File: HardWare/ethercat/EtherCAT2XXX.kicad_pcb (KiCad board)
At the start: 4 copper layers, 153 parts, among them CN1 5019530507, CN2 5019530507, J1 Conn_01x02, J2 Conn_01x03, J3 Conn_01x04, J4 Conn_01x02, J5 Conn_01x02, J6 Conn_01x03, J7 Conn_01x04, SW1 SW_Push, U1 SY8303AAIC, U2 RT8075, U3 SRV05-4, U4 SRV05-4, U5 STM32F407VETx, U6 TJA1051T-3, U7 TJA1051T-3, U8 AX58100-LQPF80, U9 BL24C16F-PARC, X1 25M, Y1 8M, Y2 32.768KHz

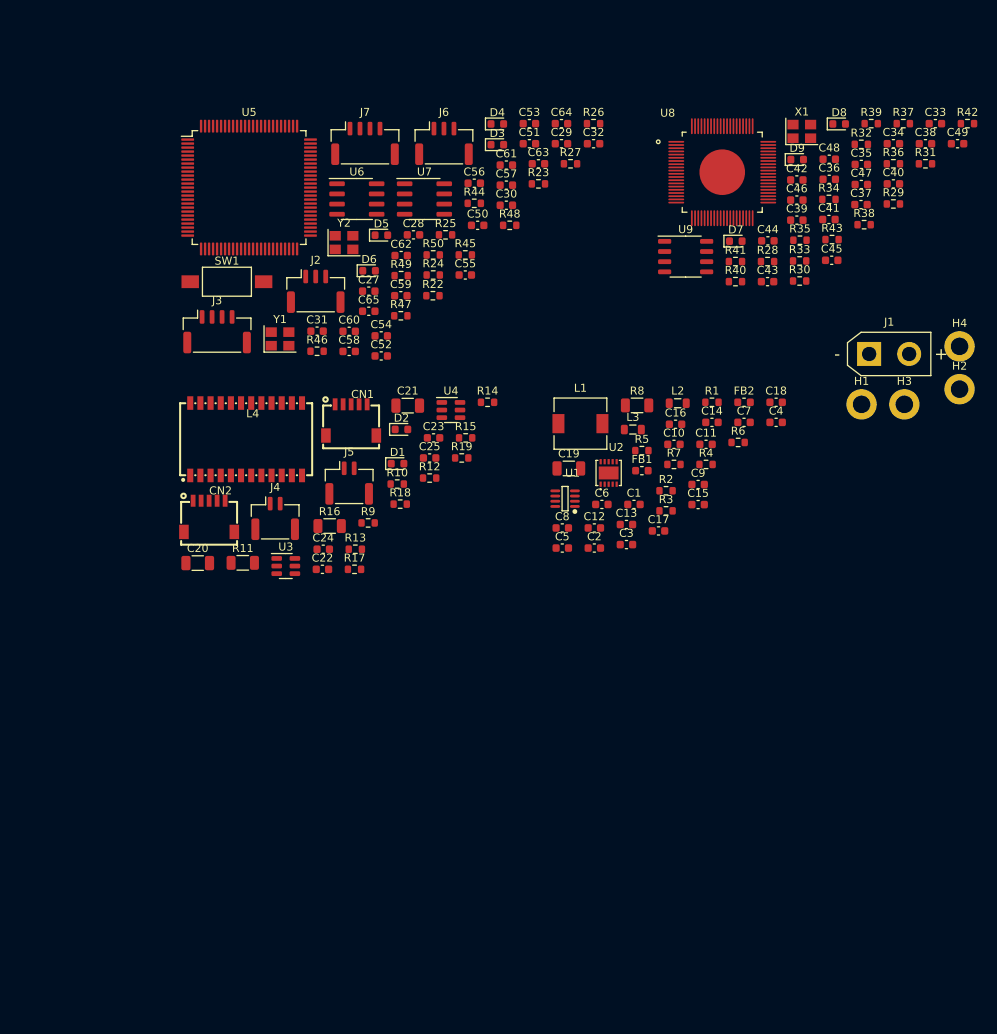
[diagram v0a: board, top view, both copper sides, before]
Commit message: 'ethercat_shield' PCB_layout completed
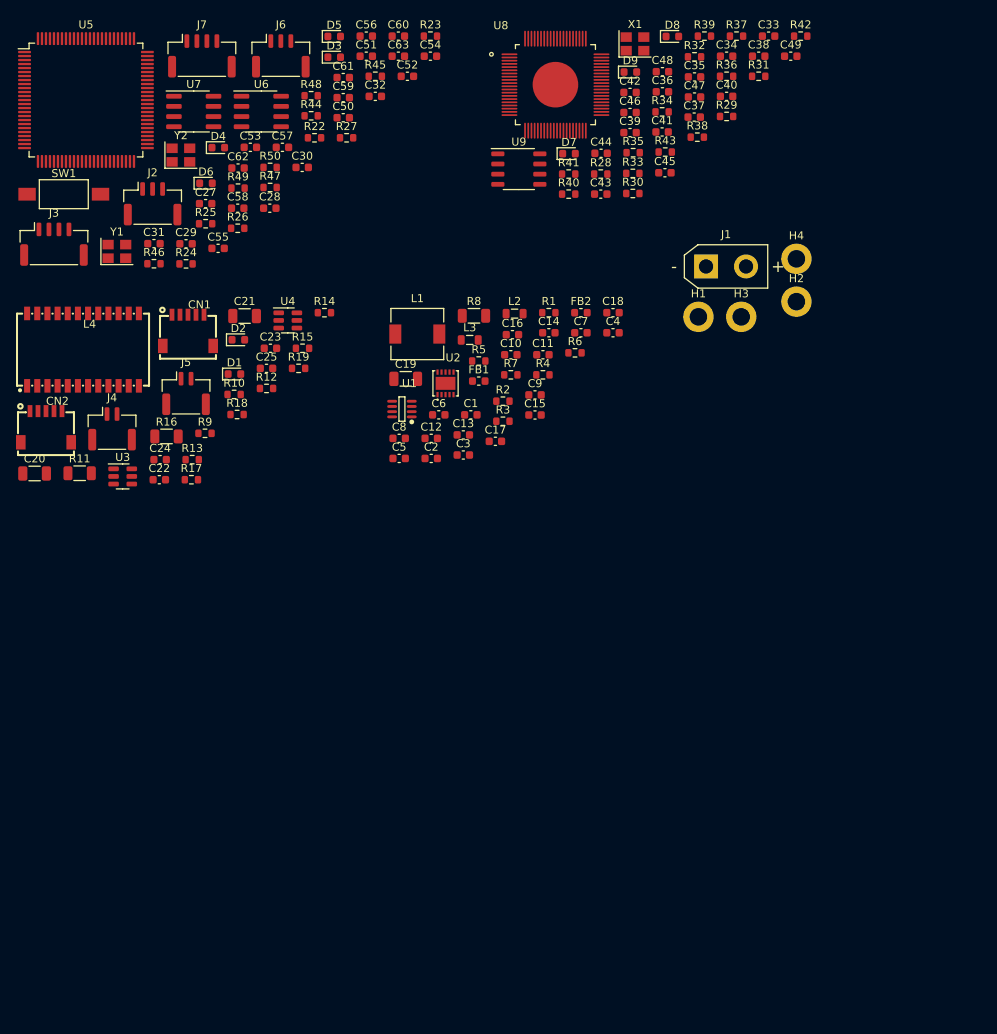
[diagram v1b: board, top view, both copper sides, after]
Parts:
- removed C64, C65: 100n, Capacitor_SMD:C_0603_1608Metric
- moved C29 48.6 mm to (40.5, 41.7)
- moved R26 46.4 mm to (46.9, 39.8)
- moved C60 37.4 mm to (67.0, 15.7)
- moved C54 35.5 mm to (71.0, 18.2)
- moved C52 35.1 mm to (68.1, 20.8)
- moved D4 35.0 mm to (44.5, 29.7)
- moved C53 35.0 mm to (48.5, 29.6)
- moved C55 31.1 mm to (44.5, 42.3)
- moved R24 30.9 mm to (40.5, 44.2)
- moved U7 30.8 mm to (41.4, 25.1)
- moved R25 30.0 mm to (42.9, 39.2)
- moved R48 29.6 mm to (56.1, 23.2)
- moved C57 28.4 mm to (52.5, 29.6)
- moved R27 28.2 mm to (60.5, 28.4)
- moved C32 27.9 mm to (64.1, 23.3)
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
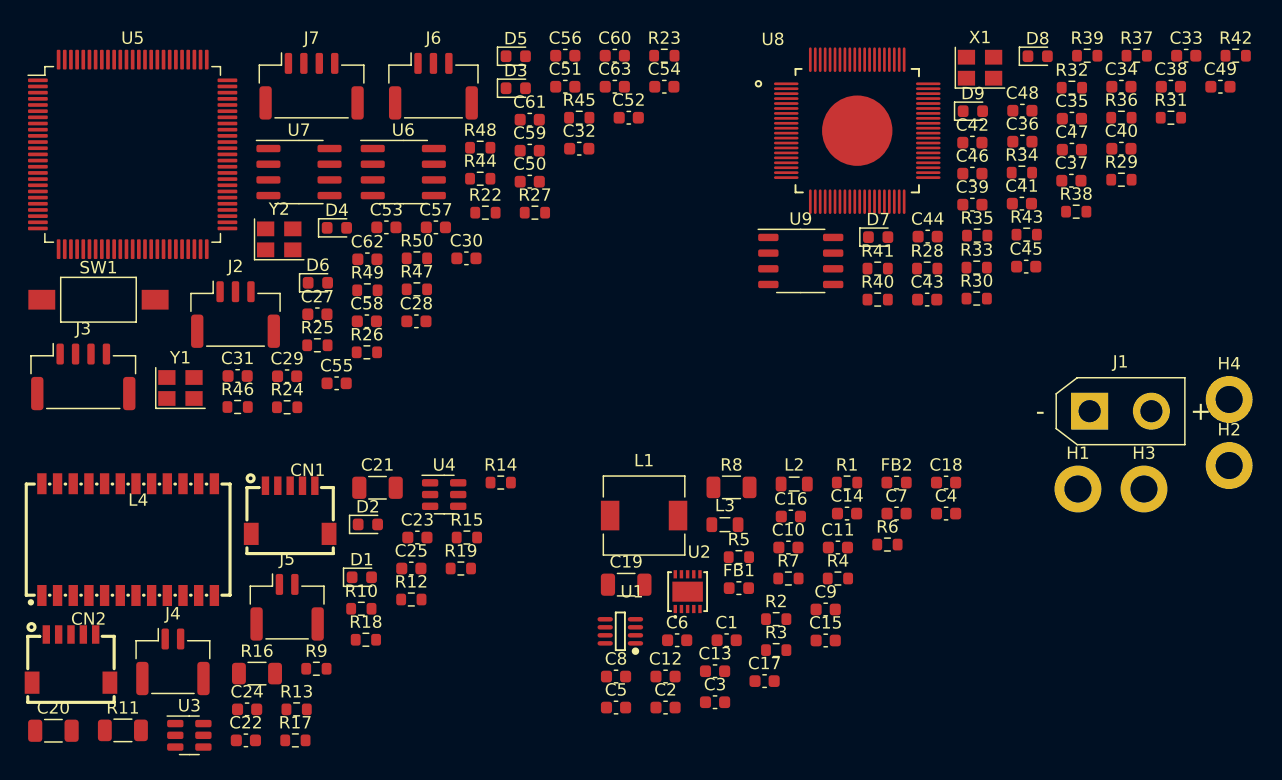
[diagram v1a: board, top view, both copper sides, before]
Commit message: Adaption for Kicad 7.0
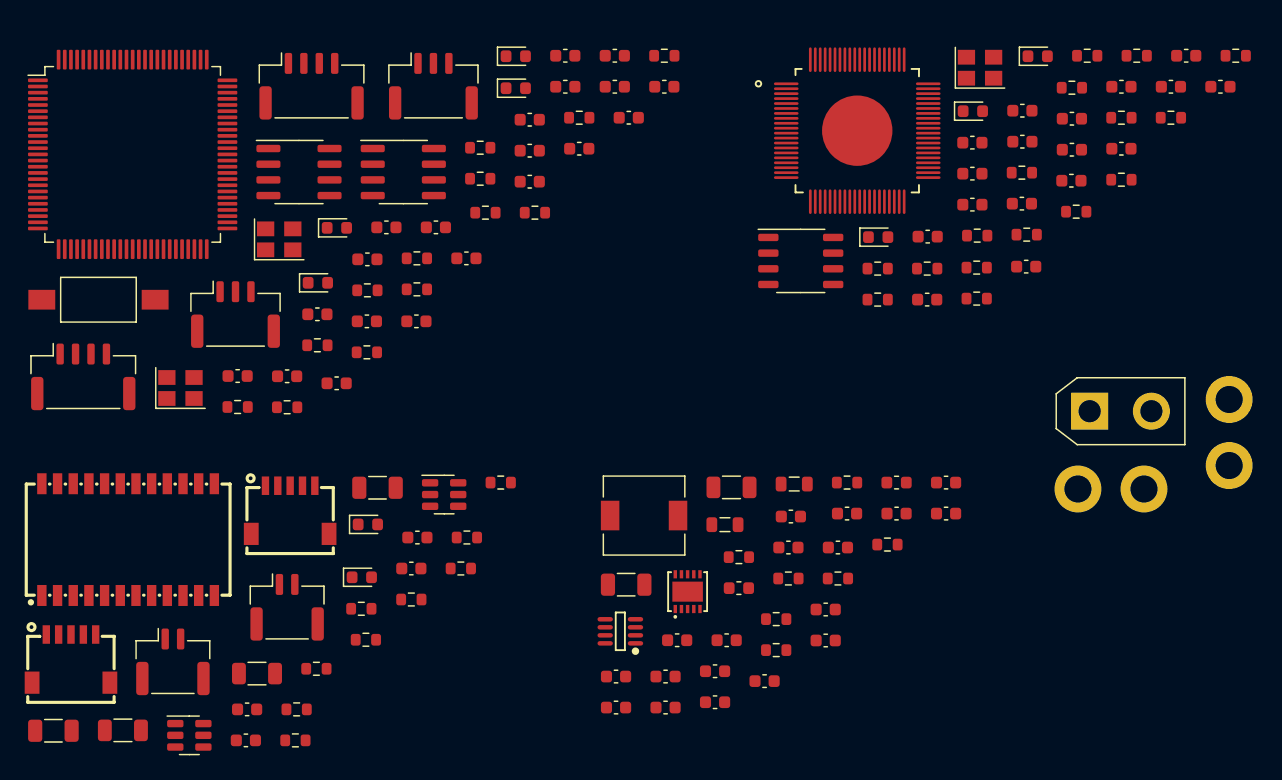
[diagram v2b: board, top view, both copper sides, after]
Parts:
- C35, C36, C37, C38, C39, C40, C41, C42, C43, C44, C45, C46, C47, C48, C49: value 100nF -> 100n

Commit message: Official version-EtherCAT2CAN_NUC
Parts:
- removed C3: 10n, Capacitor_SMD:C_0603_1608Metric
- removed C4: 22u, Capacitor_SMD:C_0603_1608Metric
- removed C50, C51: 2.2u, Capacitor_SMD:C_0603_1608Metric
- removed C52, C54: 10u, Capacitor_SMD:C_0603_1608Metric
- removed C53, C59, C61: 100n, Capacitor_SMD:C_0603_1608Metric
- removed C55, C56: 10p, Capacitor_SMD:C_0603_1608Metric
- removed H1, H2, H4: MountingHole, MountingHole:MountingHole_2.2mm_M2_DIN965_Pad
- removed the H3 at (109.9, 50.8)
- removed J2: Conn_01x03, Connector_JST:JST_GH_SM03B-GHS-TB_1x03-1MP_P1.25mm_Horizontal
- removed J3, J7: Conn_01x04, Connector_JST:JST_GH_SM04B-GHS-TB_1x04-1MP_P1.25mm_Horizontal
- removed L1: 22uH, Inductor_SMD:L_6.3x6.3_H3
- removed R25: 1K, Resistor_SMD:R_0603_1608Metric
- removed R44, R48, R49: 10K, Resistor_SMD:R_0603_1608Metric
- removed R45: 10, Resistor_SMD:R_0603_1608Metric
- removed R46, R47: 0, Resistor_SMD:R_0603_1608Metric
- removed R50: 1M, Resistor_SMD:R_0603_1608Metric
- removed SW1: SW_Push, Button_Switch_SMD:SW_SPST_FSMSM
- removed Y2: 32.768KHz, Crystal:Crystal_SMD_3225-4Pin_3.2x2.5mm
- added C64: 100n, Capacitor_SMD:C_0402_1005Metric, B.Cu at (117.2, 97.6)
- added D10: RED, LED_SMD:LED_0402_1005Metric, F.Cu at (100.6, 128.6)
- added D11: RED, LED_SMD:LED_0402_1005Metric, F.Cu at (101.6, 128.6)
- added D12: BV05C, Diode_SMD:D_SOD-323, F.Cu at (96.3, 129.6)
- added H3: MountingHole, MountingHole:MountingHole_2.7mm_M2.5, F.Cu at (127.3, 93.9)
- added H3: MountingHole, MountingHole:MountingHole_2.7mm_M2.5, F.Cu at (90.3, 93.9)
- added H3: MountingHole, MountingHole:MountingHole_2.7mm_M2.5, F.Cu at (90.3, 134.7)
- added H3: MountingHole, MountingHole:MountingHole_2.7mm_M2.5, F.Cu at (127.4, 134.6)
- added U10: STM32F412RETx, Package_QFP:LQFP-64_10x10mm_P0.5mm, F.Cu at (102.5, 104.8)
- added U11: ~, Package_TO_SOT_SMD:SOT-23-3, F.Cu at (114.5, 96.3)
- C1: value 4.7u -> 100n; footprint Capacitor_SMD:C_0603_1608Metric -> Capacitor_SMD:C_0402_1005Metric; moved to B.Cu
- C10, C13, C14, C17, C18, C27, C28, C32, C46, C6, C8, C9: footprint Capacitor_SMD:C_0603_1608Metric -> Capacitor_SMD:C_0402_1005Metric
- C2: value 10n -> 4.7u; footprint Capacitor_SMD:C_0603_1608Metric -> Capacitor_SMD:C_0402_1005Metric; moved to B.Cu
- C21, R10, R16, R17, R18, R19, R9, U6, U7, U9: moved to B.Cu
- C22, C23, C24, C25, C29, C30, C31, C35, C36, C37, C38, C39, C40, C41, C42, C43, C44, C45, C47, C48, C49, C57, C58, C60, C62, C63: footprint Capacitor_SMD:C_0603_1608Metric -> Capacitor_SMD:C_0402_1005Metric; moved to B.Cu
- C33, C34: value 100nF -> 100n; footprint Capacitor_SMD:C_0603_1608Metric -> Capacitor_SMD:C_0402_1005Metric; moved to B.Cu
- D1, D2: value LED -> GREEN; footprint LED_SMD:LED_0603_1608Metric -> LED_SMD:LED_0402_1005Metric
- D3, D4, D7, D8, D9: footprint LED_SMD:LED_0603_1608Metric -> LED_SMD:LED_0402_1005Metric
- D5: value GREEN -> BLUE; footprint LED_SMD:LED_0603_1608Metric -> LED_SMD:LED_0402_1005Metric
- D6: value GREEN -> BV05C; footprint LED_SMD:LED_0603_1608Metric -> Diode_SMD:D_SOD-323
- J1: value Conn_01x02 -> Conn_01x04; footprint Connector_AMASS:AMASS_XT30UPB-M_1x02_P5.0mm_Vertical -> Connector_JST:JST_GH_SM04B-GHS-TB_1x04-1MP_P1.25mm_Horizontal
- J6: value Conn_01x03 -> Conn_01x06; footprint Connector_JST:JST_GH_SM03B-GHS-TB_1x03-1MP_P1.25mm_Horizontal -> Connector_JST:JST_GH_SM06B-GHS-TB_1x06-1MP_P1.25mm_Horizontal
- R1: value 100K -> 10K; footprint Resistor_SMD:R_0603_1608Metric -> Resistor_SMD:R_0402_1005Metric; moved to B.Cu
- R12, R13, R14, R15, R28, R29, R31, R39, R40, R41, R42, R43: footprint Resistor_SMD:R_0603_1608Metric -> Resistor_SMD:R_0402_1005Metric; moved to B.Cu
- R2: value 150K -> 1K; footprint Resistor_SMD:R_0603_1608Metric -> Resistor_SMD:R_0402_1005Metric
- R22, R23, R24, R26, R27, R30, R32, R33, R34, R35, R36, R37: footprint Resistor_SMD:R_0603_1608Metric -> Resistor_SMD:R_0402_1005Metric
- R3: value 20.5K -> 1K; footprint Resistor_SMD:R_0603_1608Metric -> Resistor_SMD:R_0402_1005Metric
- R38: value 510 -> 2K; footprint Resistor_SMD:R_0603_1608Metric -> Resistor_SMD:R_0402_1005Metric
- R4: value 453k -> 680k; footprint Resistor_SMD:R_0603_1608Metric -> Resistor_SMD:R_0402_1005Metric
- R5: value 100K -> 150K; footprint Resistor_SMD:R_0603_1608Metric -> Resistor_SMD:R_0402_1005Metric
- R6: value 453k -> 200k; footprint Resistor_SMD:R_0603_1608Metric -> Resistor_SMD:R_0402_1005Metric
- R7: value 100K -> 200K; footprint Resistor_SMD:R_0603_1608Metric -> Resistor_SMD:R_0402_1005Metric
- U1: value SY8303AAIC -> ~; footprint EXTRA IC:SOT-23-8_L3.0-W1.7-P0.65-LS2.8-BR -> Package_TO_SOT_SMD:SOT-23-5; moved to B.Cu
- U5: value STM32F407VETx -> ~; footprint Package_QFP:LQFP-100_14x14mm_P0.5mm -> Package_TO_SOT_SMD:SOT-23-3
- X1: footprint Crystal:Crystal_SMD_3225-4Pin_3.2x2.5mm -> Crystal:Crystal_SMD_2520-4Pin_2.5x2.0mm
- moved CN1 114.6 mm to (121.5, 133.7)
- moved L4 114.5 mm to (118.6, 124.4)
- moved CN2 114.2 mm to (113.8, 133.7)
- moved D2 110.7 mm to (126.6, 130.6), turned to 90 degrees
- moved R39 110.3 mm to (126.2, 124.0)
- moved D1 109.6 mm to (128.7, 130.6), turned to 90 degrees
- moved D5 107.5 mm to (89.2, 118.9)
- moved C20 105.8 mm to (107.8, 131.7)
- moved U5 103.9 mm to (102.3, 96.3)
- moved R18 103.3 mm to (128.7, 126.0), turned to -90 degrees
- moved J6 101.9 mm to (91.3, 112.4), turned to -90 degrees
- moved C21 100.8 mm to (107.8, 131.7), turned to 180 degrees
- moved R17 100.8 mm to (125.7, 126.0), turned to -90 degrees
- moved R13 100.6 mm to (121.8, 128.9), turned to -90 degrees
- moved C22 100.5 mm to (124.3, 121.2), turned to 180 degrees
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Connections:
- C1 pad 1: VCC -> GND
- C1 pad 2: GND -> Net-(U10-NRST)
- C2 pad 1: Net-(U1-BS) -> GND
- C2 pad 2: Net-(U1-LX) -> Net-(U10-VCAP_1)
- D3 pad 1: /MCU/LED1 -> /MCU/LED_CAN1
- D4 pad 1: /MCU/LED2 -> /MCU/LED_CAN0
- D5 pad 1: /MCU/LED3 -> /MCU/LED_UART
- D6 pad 1: /MCU/LED4 -> GND
- D6 pad 2: Net-(D6-A) -> +5V
- J1 pad 1: VCC -> +5V
- J1 pad 2: GND -> unconnected-(J1-Pin_2-Pad2)
- J6 pad 1: /MCU/USART2_RX -> GND
- J6 pad 2: /MCU/USART2_TX -> /MCU/SWDIO
- J6 pad 3: GND -> /MCU/SWCLK
- R1 pad 1: Net-(U1-FS) -> GND
- R1 pad 2: GND -> Net-(U10-BOOT0)
- R2 pad 1: +5V -> Net-(D10-A)
- R2 pad 2: Net-(U1-FB) -> 3V3
- R3 pad 1: Net-(U1-FB) -> Net-(D11-A)
- R3 pad 2: GND -> 1V2
- R33 pad 2: Net-(D7-A) -> /ESC/LED_RUN
- R34 pad 2: Net-(D8-A) -> /ESC/LED_ERR
- R35 pad 2: Net-(D9-A) -> /ESC/EEP_DONE
- U1 pad 1: Net-(U1-FB) -> unconnected-(U1-NC-Pad1)
- U1 pad 2: Net-(U1-FS) -> GND
- U1 pad 3: GND -> unconnected-(U1-NC-Pad3)
- U1 pad 4: GND -> /MCU/USART_RX
- U1 pad 5: VCC -> /MCU/USART_TX
- U5 pad 1: unconnected-(U5-PE2-Pad1) -> /CONN/CAN0_H
- U5 pad 2: unconnected-(U5-PE3-Pad2) -> /CONN/CAN0_L
- U5 pad 3: unconnected-(U5-PE4-Pad3) -> GND
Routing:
- net +5V: track 0.00 -> 65.2 mm, vias 0 -> 3
- net 3V3: track 0.00 -> 51.5 mm, vias 0 -> 20
- net GND: track 0.00 -> 37.7 mm, vias 0 -> 84
- net A1V2: track 0.00 -> 32.7 mm, vias 0 -> 2
- net 1V2: track 0.00 -> 25.3 mm, vias 0 -> 11
- net /MCU/LED_UART: track 0.00 -> 22.7 mm, vias 0 -> 2
- net /ESC/RSTN: track 0.00 -> 22.3 mm
- net /MCU/USART_TX: track 0.00 -> 21.8 mm, vias 0 -> 1
- net /MCU/USART_RX: track 0.00 -> 21.6 mm, vias 0 -> 2
- net /CONN/P1_TXOP: track 0.00 -> 21.5 mm, vias 0 -> 2
- net /CONN/P1_ACT: track 0.00 -> 20.9 mm, vias 0 -> 1
- net /CONN/P1_TXON: track 0.00 -> 19.6 mm, vias 0 -> 2
- net /ESC/SCLK: track 0.00 -> 17.3 mm, vias 0 -> 2
- net /CONN/P0_ACT: track 0.00 -> 17.1 mm, vias 0 -> 1
- net /ESC/SYNC: track 0.00 -> 16.5 mm, vias 0 -> 2
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- added copper zone on F.Cu, net 1V2
- added copper zone on In2.Cu, net 1V2
- added copper zone on F.Cu, net 3V3
- added copper zone on In2.Cu, net 3V3
- added copper zone on F.Cu, net A1V2
- added copper zone on F.Cu, net A3V3
- added copper zone on In2.Cu, net A3V3
- added copper zone on B.Cu, net Earth
- added copper zone on F.Cu, net Earth
- added copper zone on In1.Cu, net Earth
- added copper zone on B.Cu, net GND
- added copper zone on F.Cu, net GND
- added copper zone on In1.Cu, net GND
- added copper zone on F.Cu, net Net-(C20-Pad2)
- added copper zone on B.Cu, net Net-(C21-Pad1)
- added copper zone on F.Cu, net Net-(U2-FB1)
- added copper zone on F.Cu, net Net-(U2-FB2)
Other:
- board outline added: 41.5 x 45.2 mm
- board text added: "1V2"
- board text added: "3V3"
- board text added: "CAN0"
- board text added: "CAN1"
- board text added: "EPP"
- board text added: "ERR"
- board text added: "EtherCAT2CAN_NUC"
- board text added: "GND DIO CLK TX RX 5V"
- board text added: "IN"
- board text added: "OUT"
- board text added: "RUN"
- board text added: "SWD UART"
